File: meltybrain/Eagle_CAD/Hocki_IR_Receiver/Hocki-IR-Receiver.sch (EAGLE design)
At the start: 63 parts, among them U1 OPA2380AIDGKR, U10 LMH6612MAX/NOPB, U11 LMH6612MAX/NOPB, U2 OPA2380AIDGKR, U3 TLV3502AIDCNR, U4 TLV3502AIDCNR, U5 SN74LVC1G58DCKR, U6 NL27WZ32USG, U7 TMUX1204DGSR, U8 LP38693MP-5.0/NOPB, U9 TLV73310PDBVT

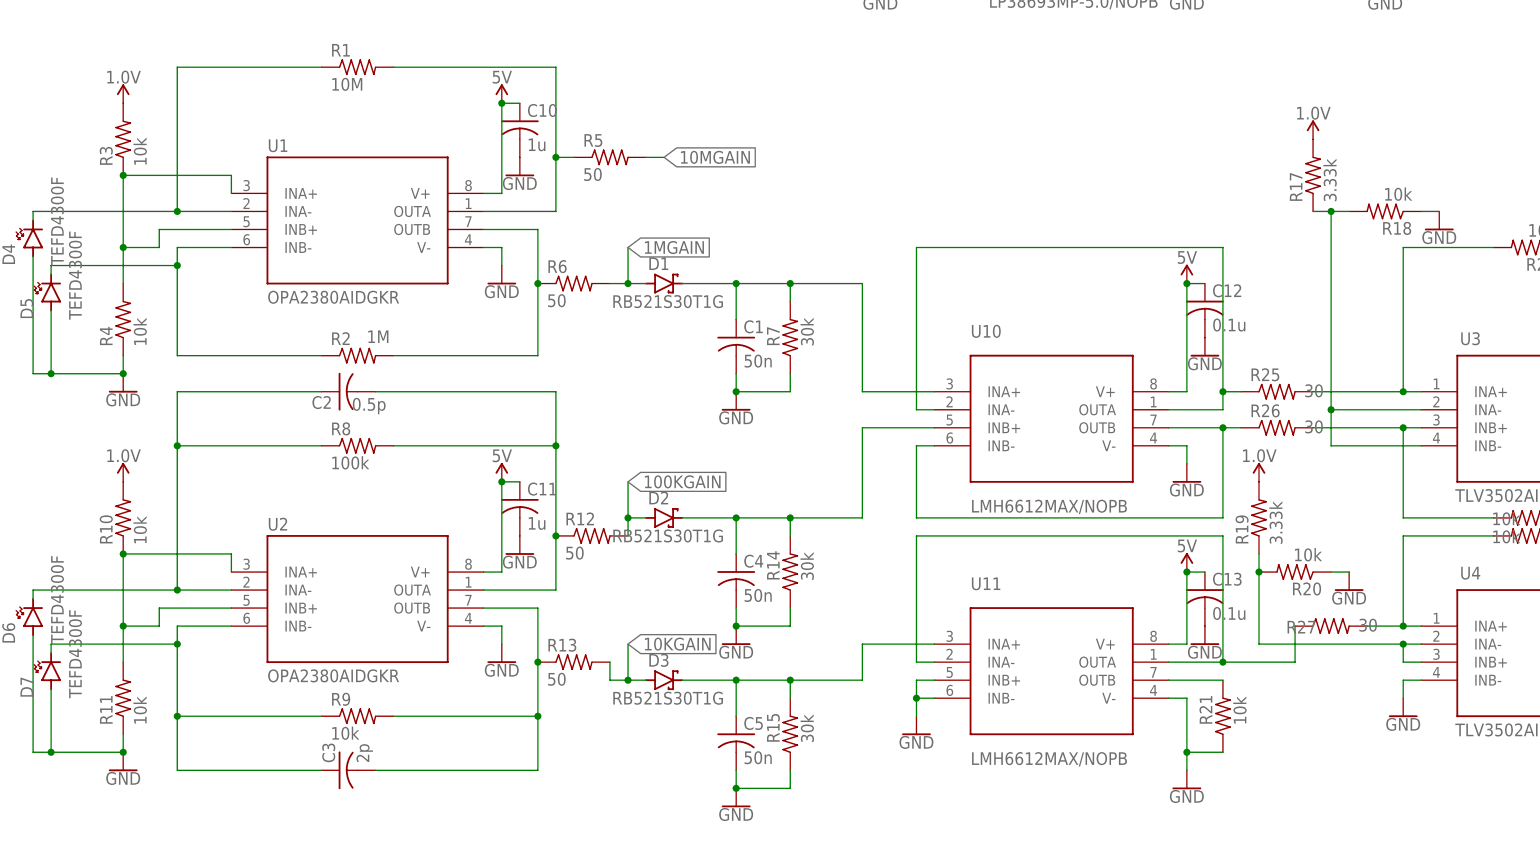
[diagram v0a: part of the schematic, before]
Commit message: added bandpass filter to control and updated ir
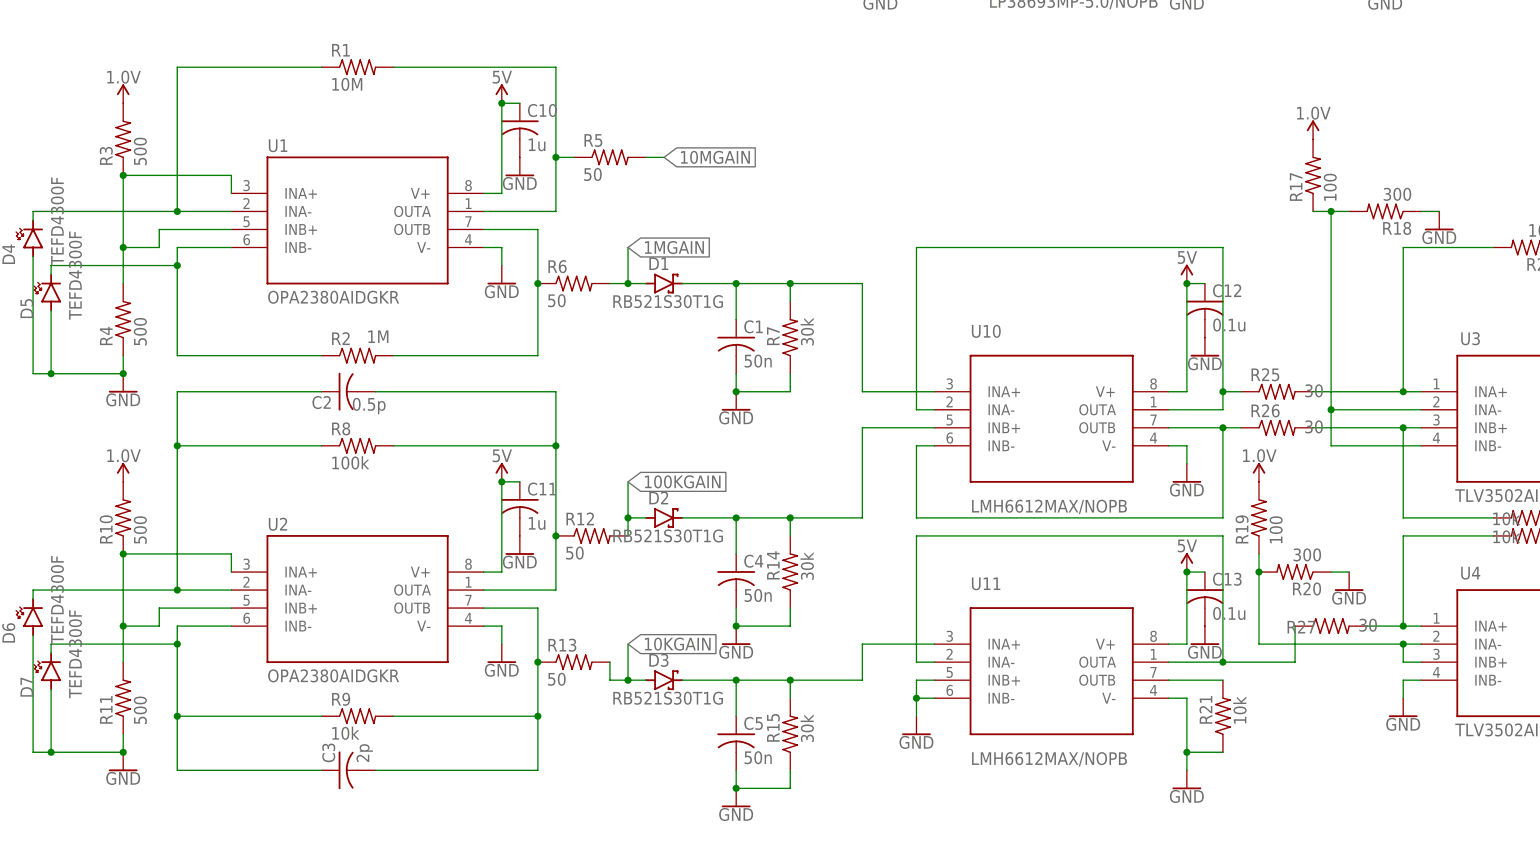
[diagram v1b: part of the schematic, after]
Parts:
- R10, R11, R3, R4: value 10k -> 500
- R17, R19: value 3.33k -> 100
- R18, R20: value 10k -> 300
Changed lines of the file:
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@@
 <part name="R2" library="resistor" library_urn="urn:adsk.eagle:library:348" deviceset="R-US_" device="R0603" package3d_urn="urn:adsk.eagle:package:26057/1" value="1M"/>
 <part name="SUPPLY1" library="SparkFun-PowerSymbols" library_urn="urn:adsk.eagle:library:530" deviceset="1.0V" device=""/>
-<part name="R3" library="resistor" library_urn="urn:adsk.eagle:library:348" deviceset="R-US_" device="R0603" package3d_urn="urn:adsk.eagle:package:26057/1" value="10k"/>
-<part name="R4" library="resistor" library_urn="urn:adsk.eagle:library:348" deviceset="R-US_" device="R0603" package3d_urn="urn:adsk.eagle:package:26057/1" value="10k"/>
+<part name="R3" library="resistor" library_urn="urn:adsk.eagle:library:348" deviceset="R-US_" device="R0603" package3d_urn="urn:adsk.eagle:package:26057/1" value="500"/>
+<part name="R4" library="resistor" library_urn="urn:adsk.eagle:library:348" deviceset="R-US_" device="R0603" package3d_urn="urn:adsk.eagle:package:26057/1" value="500"/>
 <part name="GND1" library="SparkFun-PowerSymbols" library_urn="urn:adsk.eagle:library:530" deviceset="GND" device=""/>
 <part name="SUPPLY2" library="SparkFun-PowerSymbols" library_urn="urn:adsk.eagle:library:530" deviceset="5V" device=""/>
@@
 <part name="R9" library="resistor" library_urn="urn:adsk.eagle:library:348" deviceset="R-US_" device="R0603" package3d_urn="urn:adsk.eagle:package:26057/1" value="10k"/>
 <part name="SUPPLY3" library="SparkFun-PowerSymbols" library_urn="urn:adsk.eagle:library:530" deviceset="1.0V" device=""/>
-<part name="R10" library="resistor" library_urn="urn:adsk.eagle:library:348" deviceset="R-US_" device="R0603" package3d_urn="urn:adsk.eagle:package:26057/1" value="10k"/>
-<part name="R11" library="resistor" library_urn="urn:adsk.eagle:library:348" deviceset="R-US_" device="R0603" package3d_urn="urn:adsk.eagle:package:26057/1" value="10k"/>
+<part name="R10" library="resistor" library_urn="urn:adsk.eagle:library:348" deviceset="R-US_" device="R0603" package3d_urn="urn:adsk.eagle:package:26057/1" value="500"/>
+<part name="R11" library="resistor" library_urn="urn:adsk.eagle:library:348" deviceset="R-US_" device="R0603" package3d_urn="urn:adsk.eagle:package:26057/1" value="500"/>
 <part name="GND3" library="SparkFun-PowerSymbols" library_urn="urn:adsk.eagle:library:530" deviceset="GND" device=""/>
 <part name="SUPPLY4" library="SparkFun-PowerSymbols" library_urn="urn:adsk.eagle:library:530" deviceset="5V" device=""/>
@@
 <part name="SUPPLY10" library="SparkFun-PowerSymbols" library_urn="urn:adsk.eagle:library:530" deviceset="5V" device=""/>
 <part name="U7" library="Hocki_library" deviceset="TMUX1204DGSR" device=""/>
-<part name="R17" library="resistor" library_urn="urn:adsk.eagle:library:348" deviceset="R-US_" device="R0603" package3d_urn="urn:adsk.eagle:package:26057/1" value="3.33k"/>
-<part name="R18" library="resistor" library_urn="urn:adsk.eagle:library:348" deviceset="R-US_" device="R0603" package3d_urn="urn:adsk.eagle:package:26057/1" value="10k"/>
+<part name="R17" library="resistor" library_urn="urn:adsk.eagle:library:348" deviceset="R-US_" device="R0603" package3d_urn="urn:adsk.eagle:package:26057/1" value="100"/>
+<part name="R18" library="resistor" library_urn="urn:adsk.eagle:library:348" deviceset="R-US_" device="R0603" package3d_urn="urn:adsk.eagle:package:26057/1" value="300"/>
 <part name="GND14" library="SparkFun-PowerSymbols" library_urn="urn:adsk.eagle:library:530" deviceset="GND" device=""/>
-<part name="R19" library="resistor" library_urn="urn:adsk.eagle:library:348" deviceset="R-US_" device="R0603" package3d_urn="urn:adsk.eagle:package:26057/1" value="3.33k"/>
-<part name="R20" library="resistor" library_urn="urn:adsk.eagle:library:348" deviceset="R-US_" device="R0603" package3d_urn="urn:adsk.eagle:package:26057/1" value="10k"/>
+<part name="R19" library="resistor" library_urn="urn:adsk.eagle:library:348" deviceset="R-US_" device="R0603" package3d_urn="urn:adsk.eagle:package:26057/1" value="100"/>
+<part name="R20" library="resistor" library_urn="urn:adsk.eagle:library:348" deviceset="R-US_" device="R0603" package3d_urn="urn:adsk.eagle:package:26057/1" value="300"/>
 <part name="SUPPLY11" library="SparkFun-PowerSymbols" library_urn="urn:adsk.eagle:library:530" deviceset="5V" device=""/>
 <part name="GND15" library="SparkFun-PowerSymbols" library_urn="urn:adsk.eagle:library:530" deviceset="GND" device=""/>

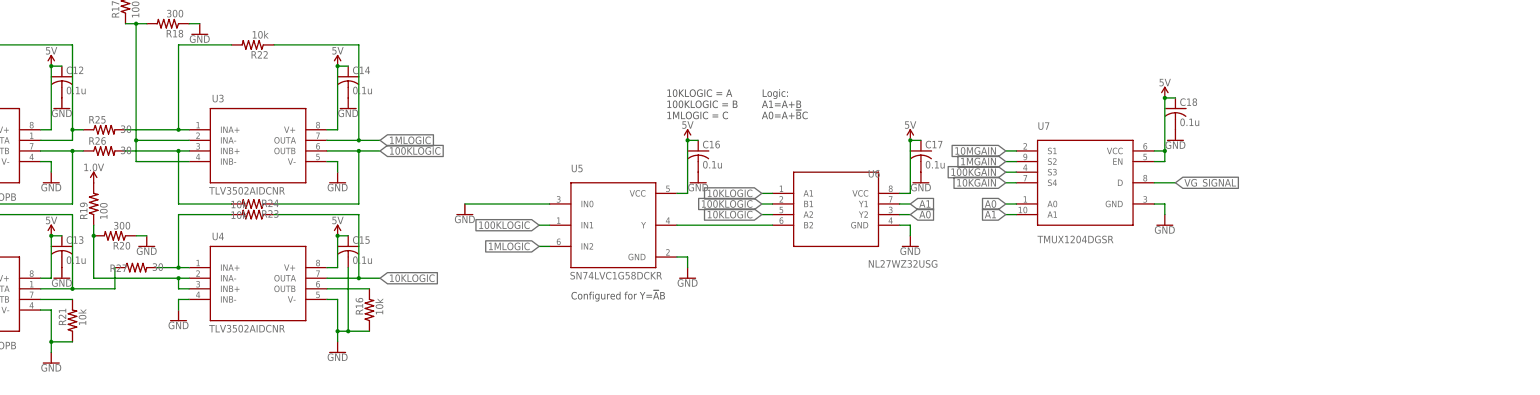
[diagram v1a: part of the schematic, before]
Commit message: Edited mutiplexers and resistors, added holes
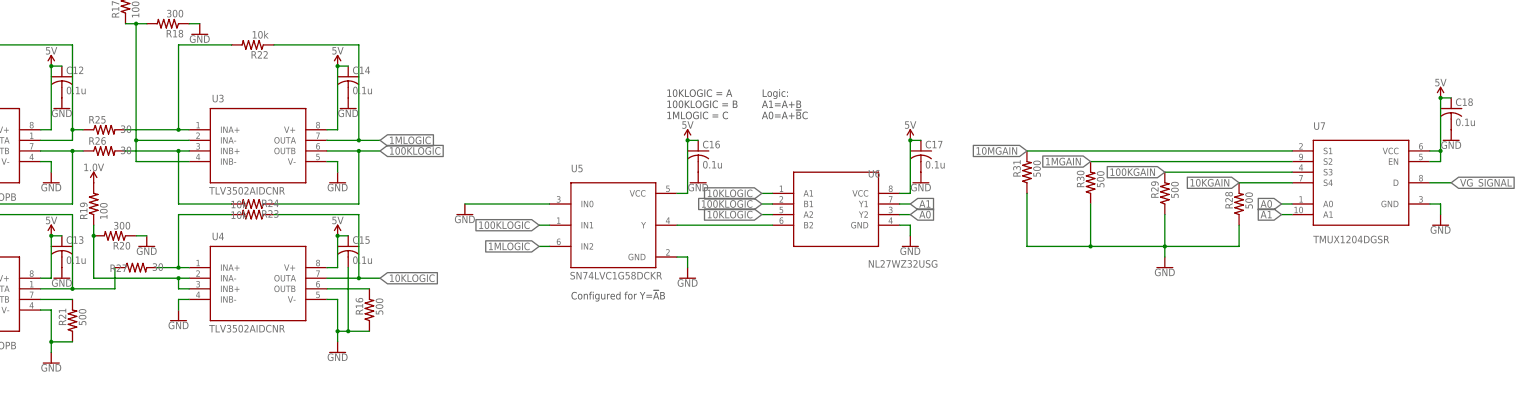
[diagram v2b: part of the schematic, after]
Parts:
- added R28, R29, R30, R31: 500, resistor:R-US_R0603
- R16, R21: value 10k -> 500
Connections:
- net 100KGAIN: now also R29.2
- net 10KGAIN: now also R28.2
- net 10MGAIN: now also R31.2
- net 1MGAIN: now also R30.2
- net GND: now also R28.1, R29.1, R30.1, R31.1
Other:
- moved on the sheet: C18, U7

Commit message: added 2:1 mux...tweaked ir layout a bit
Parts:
- D1, D2, D3: device Hocki_library:RB521S30T1G -> Hocki_Library:RB521S30T1G
- D4, D5, D6, D7: device Hocki_library:TEFD4300F -> Hocki_Library:TEFD4300F
- U1, U2: device Hocki_library:OPA2380AIDGKR -> Hocki_Library:OPA2380AIDGKR
- U10, U11: device Hocki_library:LMH6612MAX/NOPB -> Hocki_Library:LMH6612MAX/NOPB
- U3, U4: device Hocki_library:TLV3502AIDCNR -> Hocki_Library:TLV3502AIDCNR
- U5: device Hocki_library:SN74LVC1G58DCKR -> Hocki_Library:SN74LVC1G58DCKR
- U6: device Hocki_library:NL27WZ32USG -> Hocki_Library:NL27WZ32USG
- U7: device Hocki_library:TMUX1204DGSR -> Hocki_Library:TMUX1204DGSR
- U8: device Hocki_library:LP38693MP-5.0/NOPB -> Hocki_Library:LP38693MP-5.0/NOPB
- U9: device Hocki_library:TLV73310PDBVT -> Hocki_Library:TLV73310PDBVT
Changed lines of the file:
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@@
 <?xml version="1.0" encoding="utf-8"?>
 <!DOCTYPE eagle SYSTEM "eagle.dtd">
-<eagle version="9.5.1">
+<eagle version="9.5.2">
 <drawing>
 <settings>
@@
 </classes>
 <parts>
-<part name="U1" library="Hocki_library" deviceset="OPA2380AIDGKR" device=""/>
+<part name="U1" library="Hocki_Library" deviceset="OPA2380AIDGKR" device=""/>
 <part name="R1" library="resistor" library_urn="urn:adsk.eagle:library:348" deviceset="R-US_" device="R0603" package3d_urn="urn:adsk.eagle:package:26057/1" value="10M"/>
 <part name="R2" library="resistor" library_urn="urn:adsk.eagle:library:348" deviceset="R-US_" device="R0603" package3d_urn="urn:adsk.eagle:package:26057/1" value="1M"/>
@@
 <part name="R5" library="resistor" library_urn="urn:adsk.eagle:library:348" deviceset="R-US_" device="R0603" package3d_urn="urn:adsk.eagle:package:26057/1" value="50"/>
 <part name="R6" library="resistor" library_urn="urn:adsk.eagle:library:348" deviceset="R-US_" device="R0603" package3d_urn="urn:adsk.eagle:package:26057/1" value="50"/>
-<part name="D1" library="Hocki_library" deviceset="RB521S30T1G" device=""/>
+<part name="D1" library="Hocki_Library" deviceset="RB521S30T1G" device=""/>
 <part name="C1" library="rcl" library_urn="urn:adsk.eagle:library:334" deviceset="C-US" device="C0603" package3d_urn="urn:adsk.eagle:package:23616/2" value="50n"/>
 <part name="R7" library="resistor" library_urn="urn:adsk.eagle:library:348" deviceset="R-US_" device="R0603" package3d_urn="urn:adsk.eagle:package:26057/1" value="30k"/>
 <part name="GND6" library="SparkFun-PowerSymbols" library_urn="urn:adsk.eagle:library:530" deviceset="GND" device=""/>
-<part name="U2" library="Hocki_library" deviceset="OPA2380AIDGKR" device=""/>
+<part name="U2" library="Hocki_Library" deviceset="OPA2380AIDGKR" device=""/>
 <part name="R8" library="resistor" library_urn="urn:adsk.eagle:library:348" deviceset="R-US_" device="R0603" package3d_urn="urn:adsk.eagle:package:26057/1" value="100k"/>
 <part name="R9" library="resistor" library_urn="urn:adsk.eagle:library:348" deviceset="R-US_" device="R0603" package3d_urn="urn:adsk.eagle:package:26057/1" value="10k"/>
@@
 <part name="R12" library="resistor" library_urn="urn:adsk.eagle:library:348" deviceset="R-US_" device="R0603" package3d_urn="urn:adsk.eagle:package:26057/1" value="50"/>
 <part name="R13" library="resistor" library_urn="urn:adsk.eagle:library:348" deviceset="R-US_" device="R0603" package3d_urn="urn:adsk.eagle:package:26057/1" value="50"/>
-<part name="D2" library="Hocki_library" deviceset="RB521S30T1G" device=""/>
+<part name="D2" library="Hocki_Library" deviceset="RB521S30T1G" device=""/>
 <part name="C4" library="rcl" library_urn="urn:adsk.eagle:library:334" deviceset="C-US" device="C0603" package3d_urn="urn:adsk.eagle:package:23616/2" value="50n"/>
 <part name="R14" library="resistor" library_urn="urn:adsk.eagle:library:348" deviceset="R-US_" device="R0603" package3d_urn="urn:adsk.eagle:package:26057/1" value="30k"/>
@@
 <part name="C2" library="rcl" library_urn="urn:adsk.eagle:library:334" deviceset="C-US" device="C0603" package3d_urn="urn:adsk.eagle:package:23616/2" value="0.5p"/>
 <part name="C3" library="rcl" library_urn="urn:adsk.eagle:library:334" deviceset="C-US" device="C0603" package3d_urn="urn:adsk.eagle:package:23616/2" value="2p"/>
-<part name="D3" library="Hocki_library" deviceset="RB521S30T1G" device=""/>
+<part name="D3" library="Hocki_Library" deviceset="RB521S30T1G" device=""/>
 <part name="C5" library="rcl" library_urn="urn:adsk.eagle:library:334" deviceset="C-US" device="C0603" package3d_urn="urn:adsk.eagle:package:23616/2" value="50n"/>
 <part name="R15" library="resistor" library_urn="urn:adsk.eagle:library:348" deviceset="R-US_" device="R0603" package3d_urn="urn:adsk.eagle:package:26057/1" value="30k"/>
 <part name="GND7" library="SparkFun-PowerSymbols" library_urn="urn:adsk.eagle:library:530" deviceset="GND" device=""/>
-<part name="U5" library="Hocki_library" deviceset="SN74LVC1G58DCKR" device=""/>
-<part name="U6" library="Hocki_library" deviceset="NL27WZ32USG" device=""/>
-<part name="U3" library="Hocki_library" deviceset="TLV3502AIDCNR" device=""/>
-<part name="U4" library="Hocki_library" deviceset="TLV3502AIDCNR" device=""/>
+<part name="U5" library="Hocki_Library" deviceset="SN74LVC1G58DCKR" device=""/>
+<part name="U6" library="Hocki_Library" deviceset="NL27WZ32USG" device=""/>
+<part name="U3" library="Hocki_Library" deviceset="TLV3502AIDCNR" device=""/>
+<part name="U4" library="Hocki_Library" deviceset="TLV3502AIDCNR" device=""/>
 <part name="SUPPLY5" library="SparkFun-PowerSymbols" library_urn="urn:adsk.eagle:library:530" deviceset="1.0V" device=""/>
 <part name="SUPPLY6" library="SparkFun-PowerSymbols" library_urn="urn:adsk.eagle:library:530" deviceset="1.0V" device=""/>
@@
 <part name="GND13" library="SparkFun-PowerSymbols" library_urn="urn:adsk.eagle:library:530" deviceset="GND" device=""/>
 <part name="SUPPLY10" library="SparkFun-PowerSymbols" library_urn="urn:adsk.eagle:library:530" deviceset="5V" device=""/>
-<part name="U7" library="Hocki_library" deviceset="TMUX1204DGSR" device=""/>
+<part name="U7" library="Hocki_Library" deviceset="TMUX1204DGSR" device=""/>
 <part name="R17" library="resistor" library_urn="urn:adsk.eagle:library:348" deviceset="R-US_" device="R0603" package3d_urn="urn:adsk.eagle:package:26057/1" value="100"/>
 <part name="R18" library="resistor" library_urn="urn:adsk.eagle:library:348" deviceset="R-US_" device="R0603" package3d_urn="urn:adsk.eagle:package:26057/1" value="300"/>
@@
 <part name="SUPPLY11" library="SparkFun-PowerSymbols" library_urn="urn:adsk.eagle:library:530" deviceset="5V" device=""/>
 <part name="GND15" library="SparkFun-PowerSymbols" library_urn="urn:adsk.eagle:library:530" deviceset="GND" device=""/>
-<part name="U8" library="Hocki_library" deviceset="LP38693MP-5.0/NOPB" device=""/>
-<part name="U9" library="Hocki_library" deviceset="TLV73310PDBVT" device=""/>
+<part name="U8" library="Hocki_Library" deviceset="LP38693MP-5.0/NOPB" device=""/>
+<part name="U9" library="Hocki_Library" deviceset="TLV73310PDBVT" device=""/>
 <part name="SUPPLY12" library="SparkFun-PowerSymbols" library_urn="urn:adsk.eagle:library:530" deviceset="VIN" device=""/>
 <part name="SUPPLY13" library="SparkFun-PowerSymbols" library_urn="urn:adsk.eagle:library:530" deviceset="5V" device=""/>
@@
 <part name="GND19" library="SparkFun-PowerSymbols" library_urn="urn:adsk.eagle:library:530" deviceset="GND" device=""/>
 <part name="SUPPLY14" library="SparkFun-PowerSymbols" library_urn="urn:adsk.eagle:library:530" deviceset="1.0V" device=""/>
-<part name="U10" library="Hocki_library" deviceset="LMH6612MAX/NOPB" device=""/>
-<part name="U11" library="Hocki_library" deviceset="LMH6612MAX/NOPB" device=""/>
+<part name="U10" library="Hocki_Library" deviceset="LMH6612MAX/NOPB" device=""/>
+<part name="U11" library="Hocki_Library" deviceset="LMH6612MAX/NOPB" device=""/>
 <part name="SUPPLY15" library="SparkFun-PowerSymbols" library_urn="urn:adsk.eagle:library:530" deviceset="5V" device=""/>
 <part name="GND20" library="SparkFun-PowerSymbols" library_urn="urn:adsk.eagle:library:530" deviceset="GND" device=""/>
@@
 <part name="C18" library="rcl" library_urn="urn:adsk.eagle:library:334" deviceset="C-US" device="C0603" package3d_urn="urn:adsk.eagle:package:23616/2" value="0.1u"/>
 <part name="GND31" library="SparkFun-PowerSymbols" library_urn="urn:adsk.eagle:library:530" deviceset="GND" device=""/>
-<part name="D4" library="Hocki_library" deviceset="TEFD4300F" device=""/>
-<part name="D5" library="Hocki_library" deviceset="TEFD4300F" device=""/>
-<part name="D6" library="Hocki_library" deviceset="TEFD4300F" device=""/>
-<part name="D7" library="Hocki_library" deviceset="TEFD4300F" device=""/>
+<part name="D4" library="Hocki_Library" deviceset="TEFD4300F" device=""/>
+<part name="D5" library="Hocki_Library" deviceset="TEFD4300F" device=""/>
+<part name="D6" library="Hocki_Library" deviceset="TEFD4300F" device=""/>
+<part name="D7" library="Hocki_Library" deviceset="TEFD4300F" device=""/>
 <part name="R28" library="resistor" library_urn="urn:adsk.eagle:library:348" deviceset="R-US_" device="R0603" package3d_urn="urn:adsk.eagle:package:26057/1" value="500"/>
 <part name="R29" library="resistor" library_urn="urn:adsk.eagle:library:348" deviceset="R-US_" device="R0603" package3d_urn="urn:adsk.eagle:package:26057/1" value="500"/>
